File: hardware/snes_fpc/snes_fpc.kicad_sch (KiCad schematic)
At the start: 7 parts, among them J2 Connector_Generic:Conn_02x16_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, U1 74HC175, U2 74HC4078, U3 74AHC1G08, U4 74AHC1G08

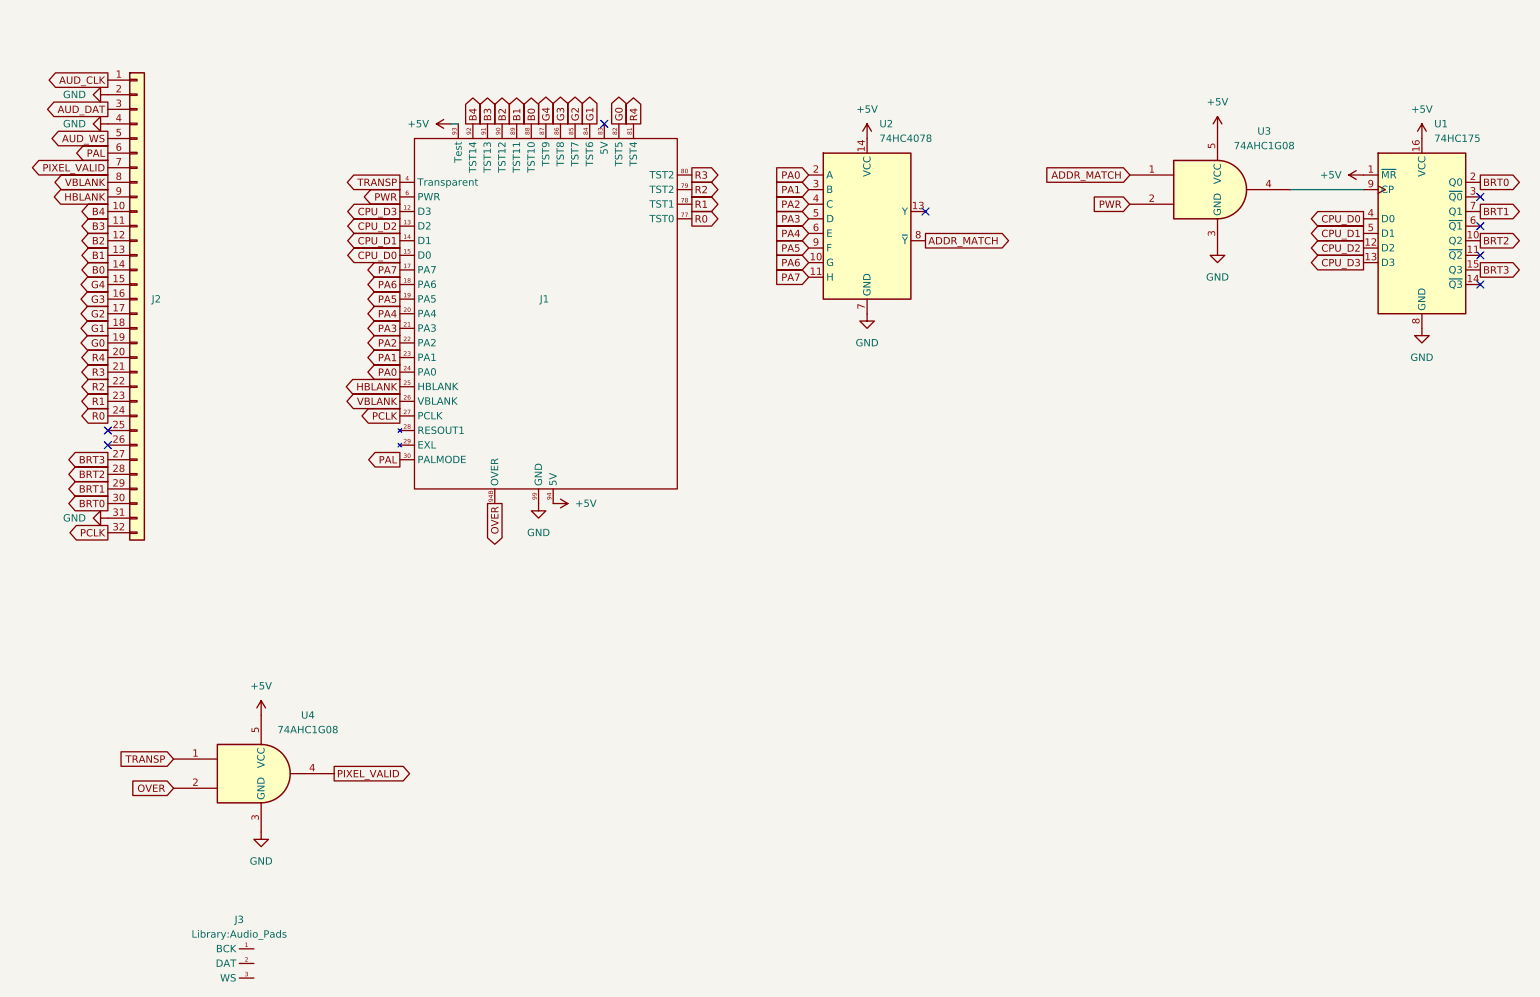
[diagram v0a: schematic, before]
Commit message: Wire missing pads
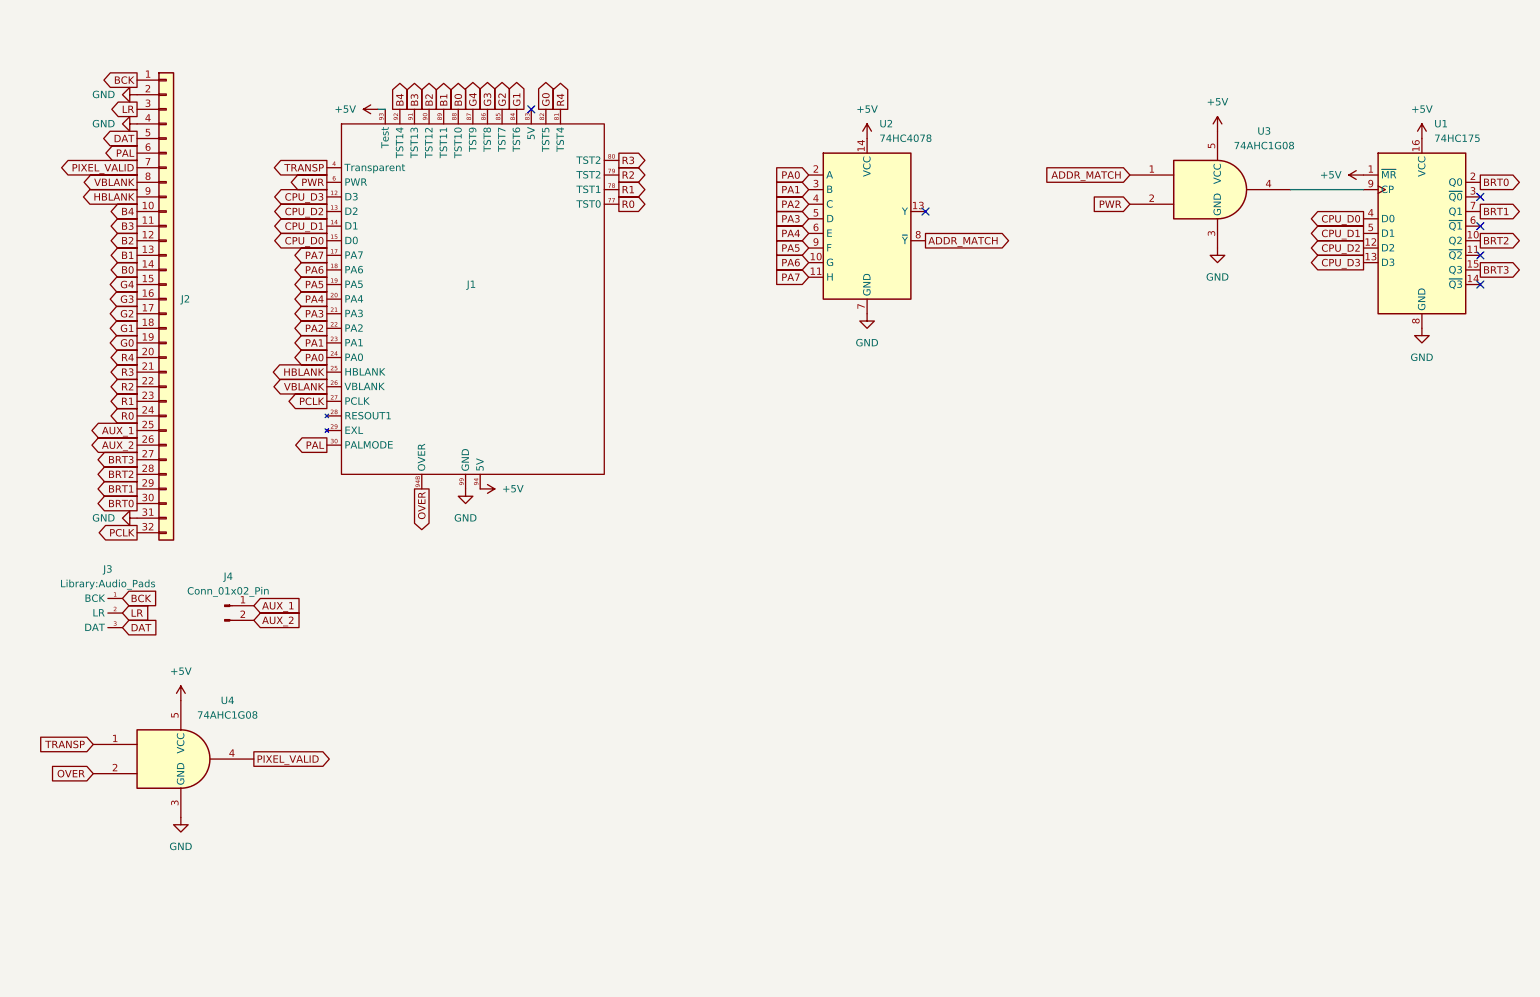
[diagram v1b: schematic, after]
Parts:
- added J4: Conn_01x02_Pin, Library:Controller_Pads, symbol Connector:Conn_01x02_Pin
- J1, J3: value ~ -> (none)
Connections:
- net AUD_CLK is gone; now on net BCK: J2.1 (Pin_1)
- net AUD_DAT is gone; now on net LR: J2.3 (Pin_3)
- net AUD_WS is gone; now on net DAT: J2.5 (Pin_5)
- net AUX_1: now reaches J2.25 (Pin_25)
- net AUX_1: now also J4.1 (Pin_1)
- net AUX_2: now reaches J2.26 (Pin_26)
- net AUX_2: now also J4.2 (Pin_2)
- net BCK: now reaches J3.1 (BCK)
- net LR: now reaches J3.2 (LR)
- net DAT: now reaches J3.3 (DAT)
- no-connect marks 8 -> 6
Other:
- moved on the sheet: J1, J2, J3, U4

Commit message: WIP footprint adjust
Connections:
- net +5V: now also J1.5 (5V)
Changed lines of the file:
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@@
 	(generator_version "10.0")
 	(paper "A4")
+	(junction
+		(at 97.79 90.17)
+		(diameter 0)
+		(color 0 0 0 0)
+	)
 	(no_connect
 		(at 269.24 44.45)
@@
 	(wire
 		(pts
+			(xy 100.33 90.17) (xy 97.79 90.17)
+		)
+		(stroke
+			(width 0)
+			(type default)
+		)
+	)
+	(wire
+		(pts
 			(xy 77.47 24.13) (xy 78.74 24.13)
 		)
@@
 	(wire
 		(pts
+			(xy 97.79 90.17) (xy 95.25 90.17)
+		)
+		(stroke
+			(width 0)
+			(type default)
+		)
+	)
+	(wire
+		(pts
+			(xy 100.33 93.98) (xy 100.33 90.17)
+		)
+		(stroke
+			(width 0)
+			(type default)
+		)
+	)
+	(wire
+		(pts
 			(xy 236.22 38.1) (xy 248.92 38.1)
 		)
@@
 		(pin "94B"
 		)
+		(pin "5"
+		)
 		(instances
 			(project "snes_fpc"
@@
 	(symbol
 		(lib_id "power:+5V")
-		(at 95.25 90.17 270)
+		(at 100.33 93.98 270)
 		(unit 1)
 		(body_style 1)
@@
 		(fields_autoplaced yes)
 		(property "Reference" "#PWR02"
-			(at 91.44 90.17 0)
+			(at 96.52 93.98 0)
 			(hide yes)
 			(show_name no)
@@
 		)
 		(property "Value" "+5V"
-			(at 99.06 90.1699 90)
+			(at 104.14 93.9799 90)
 			(show_name no)
 			(do_not_autoplace no)
@@
 		)
 		(property "Footprint" ""
-			(at 95.25 90.17 0)
+			(at 100.33 93.98 0)
 			(hide yes)
 			(show_name no)
@@
 		)
 		(property "Datasheet" ""
-			(at 95.25 90.17 0)
+			(at 100.33 93.98 0)
 			(hide yes)
 			(show_name no)
@@
 		)
 		(property "Description" "Power symbol creates a global label with name \"+5V\""
-			(at 95.25 90.17 0)
+			(at 100.33 93.98 0)
 			(hide yes)
 			(show_name no)

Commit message: Finish routing
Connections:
- net +5V: no longer J1.93 (Test), J1.94 (5V)
- net GND: now also J1.16 (GND)
- net PAL: no longer names the net of J1.30 (PALMODE)
- net PAL: no longer J2.6 (Pin_6)
- new net PPU2_5V_EXT: J1.93 (Test), J1.94 (+5V_EXT)
- no-connect marks 6 -> 8
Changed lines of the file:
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@@
 	)
 	(no_connect
+		(at 68.58 82.55)
+	)
+	(no_connect
 		(at 269.24 39.37)
 	)
@@
 	)
 	(no_connect
+		(at 35.56 31.75)
+	)
+	(no_connect
 		(at 104.14 24.13)
 	)
@@
 	(wire
 		(pts
-			(xy 77.47 24.13) (xy 78.74 24.13)
+			(xy 100.33 93.98) (xy 100.33 90.17)
 		)
 		(stroke
@@
 	(wire
 		(pts
-			(xy 97.79 90.17) (xy 95.25 90.17)
+			(xy 236.22 38.1) (xy 248.92 38.1)
 		)
 		(stroke
@@
 		)
 	)
-	(wire
-		(pts
-			(xy 100.33 93.98) (xy 100.33 90.17)
+	(global_label "PPU2_5V_EXT"
+		(shape passive)
+		(at 78.74 24.13 90)
+		(fields_autoplaced yes)
+		(effects
+			(font
+				(size 1.27 1.27)
+			)
+			(justify left)
 		)
-		(stroke
-			(width 0)
-			(type default)
+		(property "Intersheetrefs" "${INTERSHEET_REFS}"
+			(at 78.74 18.6653 90)
+			(hide yes)
+			(show_name no)
+			(do_not_autoplace no)
+			(effects
+				(font
+					(size 1.27 1.27)
+				)
+				(justify left)
+			)
 		)
 	)
-	(wire
-		(pts
-			(xy 236.22 38.1) (xy 248.92 38.1)
+	(global_label "PPU2_5V_EXT"
+		(shape passive)
+		(at 95.25 90.17 270)
+		(fields_autoplaced yes)
+		(effects
+			(font
+				(size 1.27 1.27)
+			)
+			(justify left)
 		)
-		(stroke
-			(width 0)
-			(type default)
+		(property "Intersheetrefs" "${INTERSHEET_REFS}"
+			(at 95.25 95.6347 270)
+			(hide yes)
+			(show_name no)
+			(do_not_autoplace no)
+			(effects
+				(font
+					(size 1.27 1.27)
+				)
+				(justify left)
+			)
 		)
 	)
@@
 		)
 	)
-	(global_label "PAL"
-		(shape output)
-		(at 35.56 31.75 180)
-		(fields_autoplaced yes)
-		(effects
-			(font
-				(size 1.27 1.27)
-			)
-			(justify right)
-		)
-		(property "Intersheetrefs" "${INTERSHEET_REFS}"
-			(at 29.1881 31.75 0)
-			(hide yes)
-			(show_name no)
-			(do_not_autoplace no)
-			(effects
-				(font
-					(size 1.27 1.27)
-				)
-				(justify right)
-			)
-		)
-	)
 	(global_label "G1"
 		(shape output)
@@
 		)
 	)
-	(global_label "PAL"
-		(shape output)
-		(at 68.58 82.55 180)
-		(fields_autoplaced yes)
-		(effects
-			(font
-				(size 1.27 1.27)
-			)
-			(justify right)
-		)
-		(property "Intersheetrefs" "${INTERSHEET_REFS}"
-			(at 62.2081 82.55 0)
-			(hide yes)
-			(show_name no)
-			(do_not_autoplace no)
-			(effects
-				(font
-					(size 1.27 1.27)
-				)
-				(justify right)
-			)
-		)
-	)
 	(global_label "PA7"
 		(shape output)
@@
 		(pin "5"
 		)
+		(pin "16"
+		)
 		(instances
 			(project "snes_fpc"
@@
 					(unit 1)
 				)
-			)
-		)
-	)
-	(symbol
-		(lib_id "power:+5V")
-		(at 77.47 24.13 90)
-		(unit 1)
-		(body_style 1)
-		(exclude_from_sim no)
-		(in_bom yes)
-		(on_board yes)
-		(in_pos_files yes)
-		(dnp no)
-		(fields_autoplaced yes)
-		(property "Reference" "#PWR01"
-			(at 81.28 24.13 0)
-			(hide yes)
-			(show_name no)
-			(do_not_autoplace no)
-			(effects
-				(font
-					(size 1.27 1.27)
-				)
-			)
-		)
-		(property "Value" "+5V"
-			(at 73.66 24.1299 90)
-			(show_name no)
-			(do_not_autoplace no)
-			(effects
-				(font
-					(size 1.27 1.27)
-				)
-				(justify left)
-			)
-		)
-		(property "Footprint" ""
-			(at 77.47 24.13 0)
-			(hide yes)
-			(show_name no)
-			(do_not_autoplace no)
-			(effects
-				(font
-					(size 1.27 1.27)
-				)
-			)
-		)
-		(property "Datasheet" ""
-			(at 77.47 24.13 0)
-			(hide yes)
-			(show_name no)
-			(do_not_autoplace no)
-			(effects
-				(font
-					(size 1.27 1.27)
-				)
-			)
-		)
-		(property "Description" "Power symbol creates a global label with name \"+5V\""
-			(at 77.47 24.13 0)
-			(hide yes)
-			(show_name no)
-			(do_not_autoplace no)
-			(effects
-				(font
-					(size 1.27 1.27)
-				)
-			)
-		)
-		(pin "1"
-		)
-		(instances
-			(project "snes_fpc"
-				(path "/236958bd-e58b-4f45-aaff-e27fb00ddd62"
-					(reference "#PWR01")
-					(unit 1)
-				)

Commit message: Add dec caps
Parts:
- added C1, C2, C3, C4: C_Small_US, Capacitor_SMD:C_0402_1005Metric, symbol Device:C_Small_US
- U1: JLCPCB Part # (none) -> C2682067; JLCPCB Part Type (none) -> Extended; LCSC (none) -> C2682067; LCSC Part (none) -> C2682067; LCSC Part # (none) -> C2682067; LCSC Part Name (none) -> SN74HC175PWR; MPN (none) -> SN74HC175PWR; Manufacturer (none) -> Texas Instruments; Manufacturer Part (none) -> SN74HC175PWR; Supplier (none) -> LCSC; Supplier Part (none) -> C2682067; Supplier URL (none) -> https://www.lcsc.com/product-detail/C2682067.html
- U2: value 74HC4078 -> CD4078B; JLCPCB Part # (none) -> C2682016; JLCPCB Part Type (none) -> Extended; LCSC (none) -> C2682016; LCSC Part (none) -> C2682016; LCSC Part # (none) -> C2682016; LCSC Part Name (none) -> CD4078BPWR; MPN (none) -> CD4078BPWR; Manufacturer (none) -> Texas Instruments; Manufacturer Part (none) -> CD4078BPWR; Sourcing Note (none) -> Pin-compatible TSSOP-14 LCSC/JLC 8-input OR/NOR candidate; 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; Supplier (none) -> LCSC; Supplier Part (none) -> C2682016; Supplier URL (none) -> https://www.lcsc.com/product-detail/C2682016.html
- U3, U4: JLCPCB Part # (none) -> C7467; JLCPCB Part Type (none) -> Extended; LCSC (none) -> C7467; LCSC Part (none) -> C7467; LCSC Part # (none) -> C7467; LCSC Part Name (none) -> SN74AHC1G08DBVR; MPN (none) -> SN74AHC1G08DBVR; Manufacturer (none) -> Texas Instruments; Manufacturer Part (none) -> SN74AHC1G08DBVR; Supplier (none) -> LCSC; Supplier Part (none) -> C7467; Supplier URL (none) -> https://www.lcsc.com/product-detail/Gates_Texas-Instruments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
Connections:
- net +5V: now also C1.2, C2.2, C3.2, C4.2
- net GND: now also C1.1, C2.1, C3.1, C4.1

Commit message: update fpc
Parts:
- U2: value CD4078B -> 74HC688; footprint Package_SO:TSSOP-14_4.4x5mm_P0.65mm -> Package_SO:TSSOP-20_4.4x6.5mm_P0.65mm; symbol Snes:74HC4078 -> Snes:74HC688; JLCPCB Part # C2682016 -> C132045; LCSC C2682016 -> C132045; LCSC Part C2682016 -> C132045; LCSC Part # C2682016 -> C132045; LCSC Part Name CD4078BPWR -> SN74HC688PWR; MPN CD4078BPWR -> SN74HC688PWR; Manufacturer Part CD4078BPWR -> SN74HC688PWR; Sourcing Note Pin-compatible TSSOP-14 LCSC/JLC 8-input OR/NOR candidate; 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 -> Fast HC TSSOP-20 comparator used as PA0-PA7 zero detector; 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; Supplier Part C2682016 -> C132045; Supplier URL https://www.lcsc.com/product-detail/C2682016.html -> https://www.lcsc.com/product-detail/C132045.html
- U3: value 74AHC1G08 -> 74AHC1G32; symbol 74xGxx:74AHC1G08 -> Snes:74AHC1G32; JLCPCB Part # C7467 -> C7470; LCSC C7467 -> C7470; LCSC Part C7467 -> C7470; LCSC Part # C7467 -> C7470; LCSC Part Name SN74AHC1G08DBVR -> SN74AHC1G32DBVR; MPN SN74AHC1G08DBVR -> SN74AHC1G32DBVR; Manufacturer Part SN74AHC1G08DBVR -> SN74AHC1G32DBVR; Sourcing Note (none) -> OR gate used with active-low SN74HC688 equality output and 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; Supplier Part C7467 -> C7470; Supplier URL https://www.lcsc.com/product-detail/Gates_Texas-Instruments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 -> https://www.lcsc.com/product-detail/C7470.html
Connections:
- net +5V: now also U2.20 (VCC); no longer U2.14 (VCC)
- net GND: now also U2.1 (G), U2.10 (GND), U2.12 (R4), U2.14 (R5), U2.16 (R6), U2.18 (R7), U2.3 (R0), U2.5 (R1), U2.9 (R3)
- net PA1: now also U2.4 (P1); no longer U2.3 (B)
- net PA2: now also U2.6 (P2); no longer U2.4 (C)
- net PA3: now also U2.8 (P3); no longer U2.5 (D)
- net PA4: now also U2.11 (P4); no longer U2.6 (E)
- net PA5: now also U2.13 (P5); no longer U2.9 (F)
- net PA6: now also U2.15 (P6); no longer U2.10 (G)
- net PA7: now also U2.17 (P7); no longer U2.11 (H)
- net ADDR_MATCH renamed ADDR_MATCH_N
- net ADDR_MATCH_N: now also U2.19 (P=R); no longer U2.8 (~{Y})
- no-connect marks 8 -> 7
